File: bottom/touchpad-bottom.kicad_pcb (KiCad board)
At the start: 2 copper layers, 27.5 x 18.6 mm, 6 parts, among them P1 HLW4R-2C7LF, P2 BP167911-05340H0A

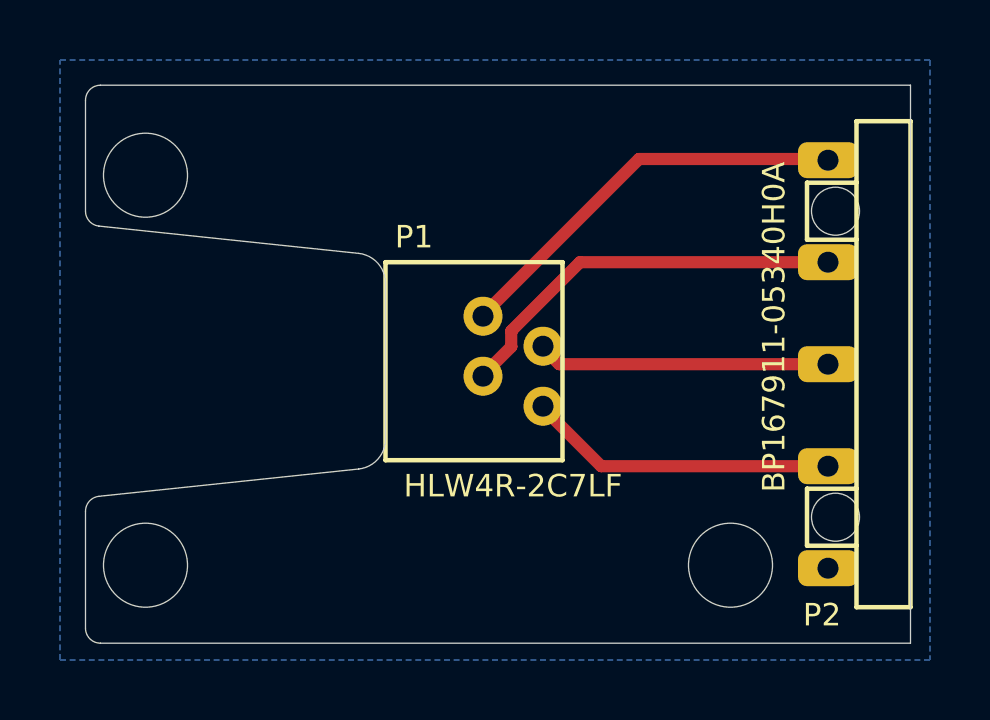
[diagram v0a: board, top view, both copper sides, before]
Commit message: Update HLW4R-2C7LF featuring enlarged annular rings and reposition the UHK logo and PCB ID text.
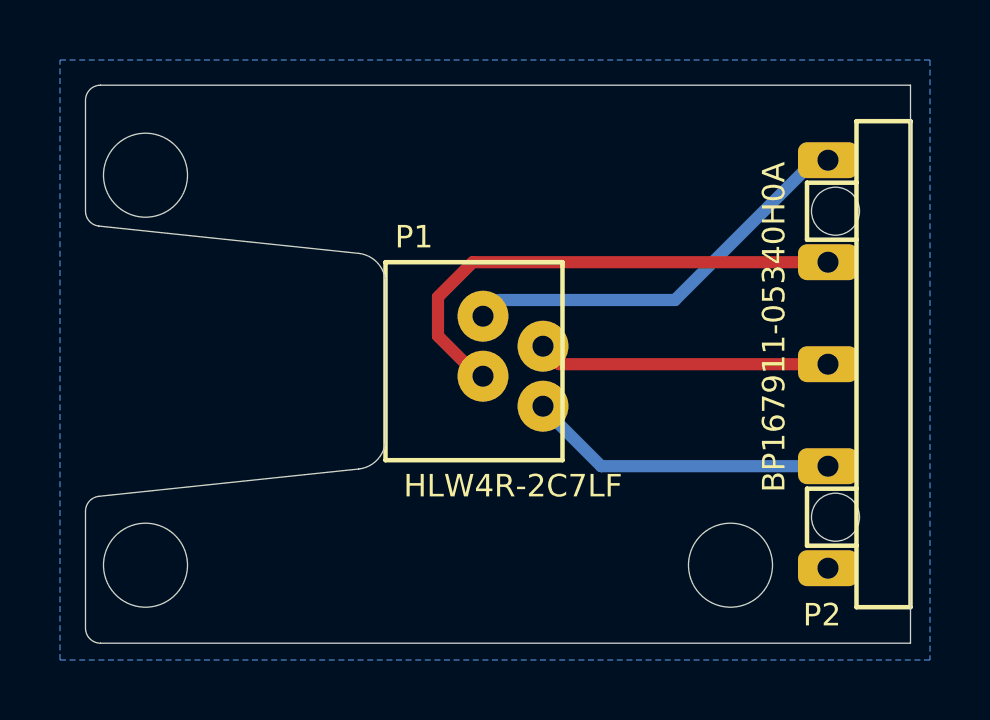
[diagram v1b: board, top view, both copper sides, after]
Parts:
- moved G*** 13.1 mm to (211.1, 136.7)
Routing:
- net /SDA: track 13.8 -> 17.3 mm
- net /VCC: track 13.7 -> 13.0 mm

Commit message: Bump the version of the bottom board to 2.2.0
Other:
- board text added: "PCB ID: touchpad_bottom_2.2.0"
- board text removed: "PCB ID: touchpad_bottom_2.1.0"
